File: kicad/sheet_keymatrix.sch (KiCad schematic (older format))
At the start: 67 parts, among them SW10 SW_Push, SW11 SW_Push, SW12 SW_Push, SW13 SW_Push, SW14 SW_Push, SW15 SW_Push, SW16 SW_Push, SW17 SW_Push, SW18 SW_Push, SW19 SW_Push, SW2 SW_Push, SW20 SW_Push, SW21 SW_Push, SW22 SW_Push, SW23 SW_Push, SW24 SW_Push, SW25 SW_Push, SW26 SW_Push, SW27 SW_Push, SW28 SW_Push, SW29 SW_Push, SW3 SW_Push, SW30 SW_Push, SW31 SW_Push, SW32 SW_Push, SW33 SW_Push, SW34 SW_Push, SW35 SW_Push, SW36 SW_Push, SW37 SW_Push, SW38 SW_Push, SW39 SW_Push, SW4 SW_Push, SW40 SW_Push, SW41 SW_Push, SW42 SW_Push, SW43 SW_Push, SW44 SW_Push, SW45 SW_Push, SW46 SW_Push, SW47 SW_Push, SW48 SW_Push, SW49 SW_Push, SW5 SW_Push, SW50 SW_Push, SW51 SW_Push, SW52 SW_Push, SW53 SW_Push, SW6 SW_Push, SW7 SW_Push, SW8 SW_Push, SW9 SW_Push

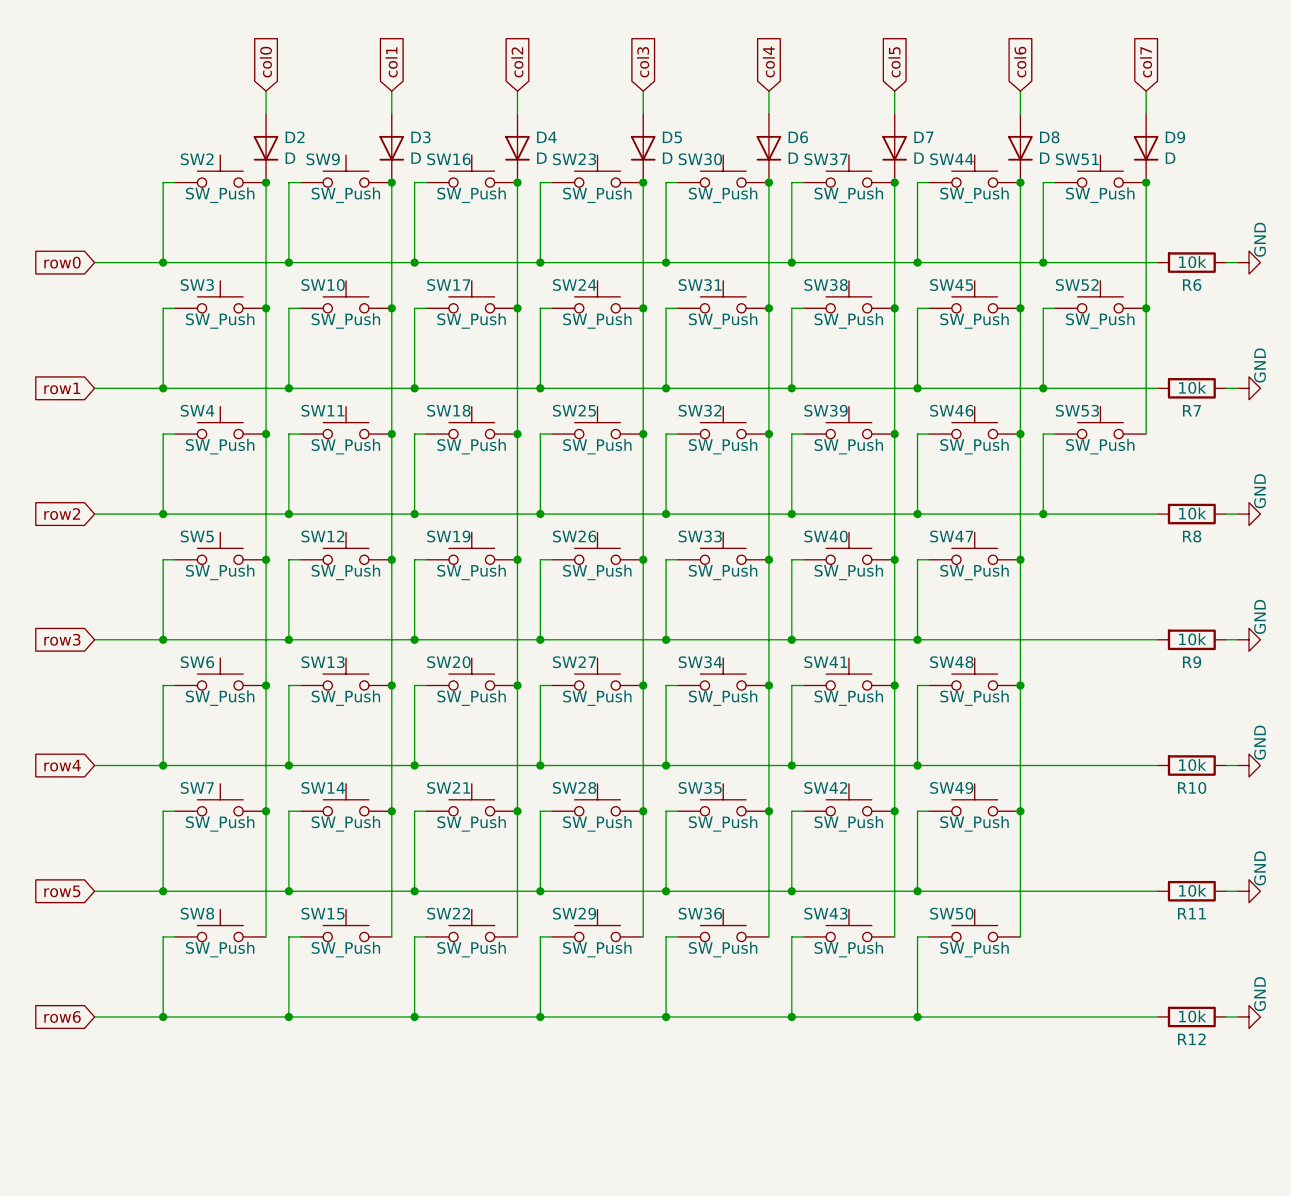
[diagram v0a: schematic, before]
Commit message: kicad: completed partial layout
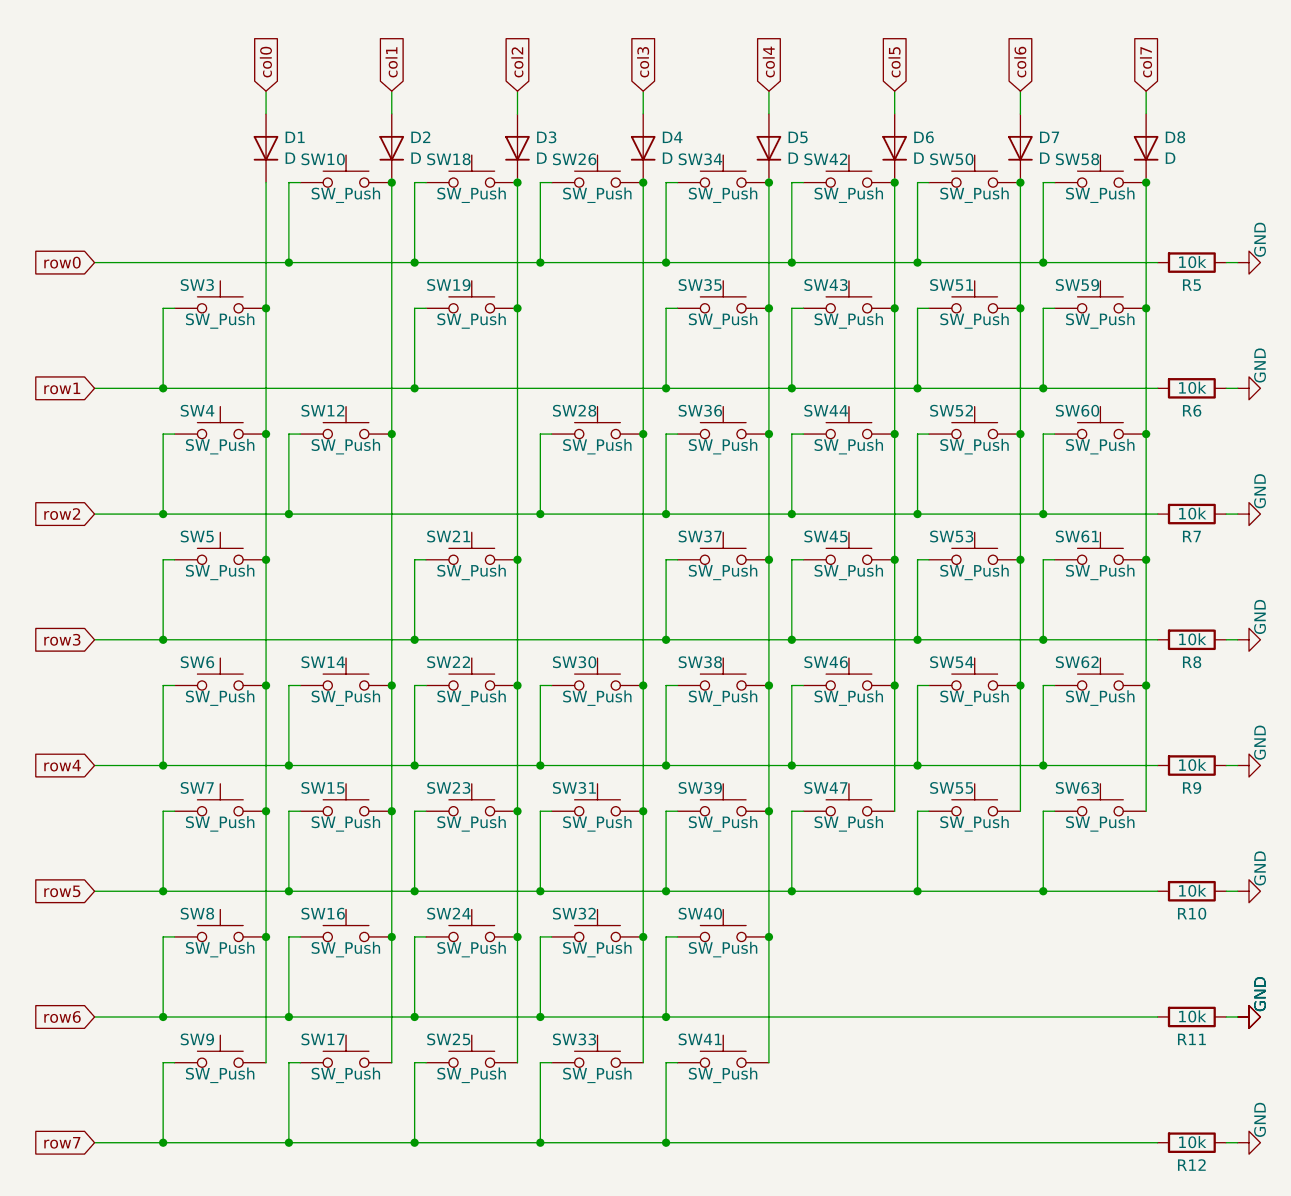
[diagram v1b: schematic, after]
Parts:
- removed SW10, SW12, SW2: SW_Push, pcb_buttons:btn_rect, symbol Switch:SW_Push
- removed SW18, SW24, SW26, SW43, SW50: SW_Push, pcb_buttons:btn_circular, symbol Switch:SW_Push
- added R12: 10k, Resistor_SMD:R_0603_1608Metric_Pad1.05x0.95mm_HandSolder, symbol Device:R
- added SW17, SW25, SW33, SW41, SW61, SW62, SW63, SW9: SW_Push, pcb_buttons:btn_circular, symbol Switch:SW_Push
- SW12: renamed from SW11; footprint pcb_buttons:btn_rect -> pcb_buttons:btn_long_rect
- SW14: renamed from SW13; footprint pcb_buttons:btn_rect -> pcb_buttons:btn_circular
- SW15: renamed from SW14; footprint pcb_buttons:btn_long_rect -> pcb_buttons:btn_circular
- SW16: renamed from SW15; footprint pcb_buttons:btn_long_rect -> pcb_buttons:btn_circular
- SW18: renamed from SW16; footprint pcb_buttons:btn_circular -> pcb_buttons:btn_rect
- SW19: renamed from SW17; footprint pcb_buttons:btn_circular -> pcb_buttons:btn_rect
- SW21: renamed from SW19; footprint pcb_buttons:btn_circular -> pcb_buttons:btn_rect
- SW26: renamed from SW23; footprint pcb_buttons:btn_circular -> pcb_buttons:btn_rect
- SW28: renamed from SW25; footprint pcb_buttons:btn_circular -> pcb_buttons:btn_long_rect
- SW34: renamed from SW30; footprint pcb_buttons:btn_circular -> pcb_buttons:btn_rect
- SW35: renamed from SW31; footprint pcb_buttons:btn_circular -> pcb_buttons:btn_rect
- SW36: renamed from SW32; footprint pcb_buttons:btn_circular -> pcb_buttons:btn_rect
- SW37: renamed from SW33; footprint pcb_buttons:btn_circular -> pcb_buttons:btn_rect
- SW6, SW7, SW8: footprint pcb_buttons:btn_rect -> pcb_buttons:btn_circular
- renumbered D2 to D1, D3 to D2, D4 to D3, D5 to D4, D6 to D5, D7 to D6, D8 to D7, D9 to D8, R11 to R10, R12 to R11, R6 to R5, R7 to R6, R8 to R7, R9 to R8, R10 to R9, SW9 to SW10, SW20 to SW22, SW21 to SW23, SW22 to SW24, SW27 to SW30, SW28 to SW31, SW29 to SW32, SW34 to SW38, SW35 to SW39, SW36 to SW40, SW37 to SW42, SW38 to SW43, SW39 to SW44, SW40 to SW45, SW41 to SW46, SW42 to SW47, SW44 to SW50, SW45 to SW51, SW46 to SW52, SW47 to SW53, SW48 to SW54, SW49 to SW55, SW51 to SW58, SW52 to SW59, SW53 to SW60
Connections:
- net GND: now also R12.1
- net row3: now also SW61.1
- net row4: now also SW62.1
- net row5: now also SW63.1
- net at D4.1 (K), SW26.2, SW28.2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: now also SW33.2
- net at D3.1 (K), SW18.2, SW19.2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: now also SW25.2
- net at D2.1 (K), SW10.2, SW12.2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: now also SW17.2
- net at D1.1 (K), SW3.2, SW4.2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: now also SW9.2
- net at D8.1 (K), SW58.2, SW59.2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: now also SW61.2, SW62.2, SW63.2
- net at D5.1 (K), SW34.2, SW35.2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: now also SW41.2
- new net row7: R12.2, SW17.1, SW25.1, SW33.1, SW41.1, SW9.1

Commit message: kicad: finalize device BOM
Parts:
- D1, D2, D3, D4, D5, D6, D7, D8: Description (none) -> Switch matrix protection; Digi-Key PN (none) -> TS4148CRZGCT-ND; Digi-Key Page (none) -> https://www.digikey.com/product-detail/en/taiwan-semiconduc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
- R10, R11, R12, R5, R6, R7, R8, R9: Description (none) -> Input pull-down resistor; Digi-Key PN (none) -> 311-10.0KHRCT-ND; Digi-Key Page (none) -> https://www.digikey.com/product-detail/en/yageo/RC0603FR-07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
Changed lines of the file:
@@
 F 1 "10k" V 5850 4850 50  0000 C CNN
 F 2 "Resistor_SMD:R_0603_1608Metric_Pad1.05x0.95mm_HandSolder" V 5780 4850 50  0001 C CNN
-F 3 "~" H 5850 4850 50  0001 C CNN
+F 3 "http://www.yageo.com/documents/recent/PYu-RC_Group_51_RoHS_L_10.pdf" H 5850 4850 50  0001 C CNN
+F 4 "Input pull-down resistor" H 5850 4850 50  0001 C CNN "Description"
+F 5 "311-10.0KHRCT-ND" H 5850 4850 50  0001 C CNN "Digi-Key PN"
+F 6 "https://www.digikey.com/product-detail/en/yageo/RC0603FR-0710KL/311-10.0KHRCT-ND/729827" H 5850 4850 50  0001 C CNN "Digi-Key Page"
 	1    5850 4850
 	0    1    1    0
@@
 F 1 "10k" V 5850 4300 50  0000 C CNN
 F 2 "Resistor_SMD:R_0603_1608Metric_Pad1.05x0.95mm_HandSolder" V 5780 4300 50  0001 C CNN
-F 3 "~" H 5850 4300 50  0001 C CNN
+F 3 "http://www.yageo.com/documents/recent/PYu-RC_Group_51_RoHS_L_10.pdf" H 5850 4300 50  0001 C CNN
+F 4 "Input pull-down resistor" H 5850 4300 50  0001 C CNN "Description"
+F 5 "311-10.0KHRCT-ND" H 5850 4300 50  0001 C CNN "Digi-Key PN"
+F 6 "https://www.digikey.com/product-detail/en/yageo/RC0603FR-0710KL/311-10.0KHRCT-ND/729827" H 5850 4300 50  0001 C CNN "Digi-Key Page"
 	1    5850 4300
 	0    1    1    0
@@
 F 1 "10k" V 5850 3750 50  0000 C CNN
 F 2 "Resistor_SMD:R_0603_1608Metric_Pad1.05x0.95mm_HandSolder" V 5780 3750 50  0001 C CNN
-F 3 "~" H 5850 3750 50  0001 C CNN
+F 3 "http://www.yageo.com/documents/recent/PYu-RC_Group_51_RoHS_L_10.pdf" H 5850 3750 50  0001 C CNN
+F 4 "Input pull-down resistor" H 5850 3750 50  0001 C CNN "Description"
+F 5 "311-10.0KHRCT-ND" H 5850 3750 50  0001 C CNN "Digi-Key PN"
+F 6 "https://www.digikey.com/product-detail/en/yageo/RC0603FR-0710KL/311-10.0KHRCT-ND/729827" H 5850 3750 50  0001 C CNN "Digi-Key Page"
 	1    5850 3750
 	0    1    1    0
@@
 F 1 "10k" V 5850 3200 50  0000 C CNN
 F 2 "Resistor_SMD:R_0603_1608Metric_Pad1.05x0.95mm_HandSolder" V 5780 3200 50  0001 C CNN
-F 3 "~" H 5850 3200 50  0001 C CNN
+F 3 "http://www.yageo.com/documents/recent/PYu-RC_Group_51_RoHS_L_10.pdf" H 5850 3200 50  0001 C CNN
+F 4 "Input pull-down resistor" H 5850 3200 50  0001 C CNN "Description"
+F 5 "311-10.0KHRCT-ND" H 5850 3200 50  0001 C CNN "Digi-Key PN"
+F 6 "https://www.digikey.com/product-detail/en/yageo/RC0603FR-0710KL/311-10.0KHRCT-ND/729827" H 5850 3200 50  0001 C CNN "Digi-Key Page"
 	1    5850 3200
 	0    1    1    0
@@
 F 1 "10k" V 5850 2650 50  0000 C CNN
 F 2 "Resistor_SMD:R_0603_1608Metric_Pad1.05x0.95mm_HandSolder" V 5780 2650 50  0001 C CNN
-F 3 "~" H 5850 2650 50  0001 C CNN
+F 3 "http://www.yageo.com/documents/recent/PYu-RC_Group_51_RoHS_L_10.pdf" H 5850 2650 50  0001 C CNN
+F 4 "Input pull-down resistor" H 5850 2650 50  0001 C CNN "Description"
+F 5 "311-10.0KHRCT-ND" H 5850 2650 50  0001 C CNN "Digi-Key PN"
+F 6 "https://www.digikey.com/product-detail/en/yageo/RC0603FR-0710KL/311-10.0KHRCT-ND/729827" H 5850 2650 50  0001 C CNN "Digi-Key Page"
 	1    5850 2650
 	0    1    1    0
@@
 F 1 "10k" V 5850 2100 50  0000 C CNN
 F 2 "Resistor_SMD:R_0603_1608Metric_Pad1.05x0.95mm_HandSolder" V 5780 2100 50  0001 C CNN
-F 3 "~" H 5850 2100 50  0001 C CNN
+F 3 "http://www.yageo.com/documents/recent/PYu-RC_Group_51_RoHS_L_10.pdf" H 5850 2100 50  0001 C CNN
+F 4 "Input pull-down resistor" H 5850 2100 50  0001 C CNN "Description"
+F 5 "311-10.0KHRCT-ND" H 5850 2100 50  0001 C CNN "Digi-Key PN"
+F 6 "https://www.digikey.com/product-detail/en/yageo/RC0603FR-0710KL/311-10.0KHRCT-ND/729827" H 5850 2100 50  0001 C CNN "Digi-Key Page"
 	1    5850 2100
 	0    1    1    0
@@
 F 1 "10k" V 5850 1550 50  0000 C CNN
 F 2 "Resistor_SMD:R_0603_1608Metric_Pad1.05x0.95mm_HandSolder" V 5780 1550 50  0001 C CNN
-F 3 "~" H 5850 1550 50  0001 C CNN
+F 3 "http://www.yageo.com/documents/recent/PYu-RC_Group_51_RoHS_L_10.pdf" H 5850 1550 50  0001 C CNN
+F 4 "Input pull-down resistor" H 5850 1550 50  0001 C CNN "Description"
+F 5 "311-10.0KHRCT-ND" H 5850 1550 50  0001 C CNN "Digi-Key PN"
+F 6 "https://www.digikey.com/product-detail/en/yageo/RC0603FR-0710KL/311-10.0KHRCT-ND/729827" H 5850 1550 50  0001 C CNN "Digi-Key Page"
 	1    5850 1550
 	0    1    1    0
@@
 F 1 "D" V 2855 971 50  0000 R CNN
 F 2 "Diode_SMD:D_0603_1608Metric_Pad1.05x0.95mm_HandSolder" H 2900 1050 50  0001 C CNN
-F 3 "~" H 2900 1050 50  0001 C CNN
+F 3 "https://www.taiwansemi.com/products/datasheet/TS4148C_G1809.pdf" H 2900 1050 50  0001 C CNN
+F 4 "Switch matrix protection" H 2900 1050 50  0001 C CNN "Description"
+F 5 "TS4148CRZGCT-ND" H 2900 1050 50  0001 C CNN "Digi-Key PN"
+F 6 "https://www.digikey.com/product-detail/en/taiwan-semiconductor-corporation/TS4148C-RZG/TS4148CRZGCT-ND/7359812" H 2900 1050 50  0001 C CNN "Digi-Key Page"
 	1    2900 1050
 	0    -1   -1   0
@@
 F 1 "D" V 3405 971 50  0000 R CNN
 F 2 "Diode_SMD:D_0603_1608Metric_Pad1.05x0.95mm_HandSolder" H 3450 1050 50  0001 C CNN
-F 3 "~" H 3450 1050 50  0001 C CNN
+F 3 "https://www.taiwansemi.com/products/datasheet/TS4148C_G1809.pdf" H 3450 1050 50  0001 C CNN
+F 4 "Switch matrix protection" H 3450 1050 50  0001 C CNN "Description"
+F 5 "TS4148CRZGCT-ND" H 3450 1050 50  0001 C CNN "Digi-Key PN"
+F 6 "https://www.digikey.com/product-detail/en/taiwan-semiconductor-corporation/TS4148C-RZG/TS4148CRZGCT-ND/7359812" H 3450 1050 50  0001 C CNN "Digi-Key Page"
 	1    3450 1050
 	0    -1   -1   0
@@
 F 1 "D" V 4505 971 50  0000 R CNN
 F 2 "Diode_SMD:D_0603_1608Metric_Pad1.05x0.95mm_HandSolder" H 4550 1050 50  0001 C CNN
-F 3 "~" H 4550 1050 50  0001 C CNN
+F 3 "https://www.taiwansemi.com/products/datasheet/TS4148C_G1809.pdf" H 4550 1050 50  0001 C CNN
+F 4 "Switch matrix protection" H 4550 1050 50  0001 C CNN "Description"
+F 5 "TS4148CRZGCT-ND" H 4550 1050 50  0001 C CNN "Digi-Key PN"
+F 6 "https://www.digikey.com/product-detail/en/taiwan-semiconductor-corporation/TS4148C-RZG/TS4148CRZGCT-ND/7359812" H 4550 1050 50  0001 C CNN "Digi-Key Page"
 	1    4550 1050
 	0    -1   -1   0
@@
 F 1 "D" V 5055 971 50  0000 R CNN
 F 2 "Diode_SMD:D_0603_1608Metric_Pad1.05x0.95mm_HandSolder" H 5100 1050 50  0001 C CNN
-F 3 "~" H 5100 1050 50  0001 C CNN
+F 3 "https://www.taiwansemi.com/products/datasheet/TS4148C_G1809.pdf" H 5100 1050 50  0001 C CNN
+F 4 "Switch matrix protection" H 5100 1050 50  0001 C CNN "Description"
+F 5 "TS4148CRZGCT-ND" H 5100 1050 50  0001 C CNN "Digi-Key PN"
+F 6 "https://www.digikey.com/product-detail/en/taiwan-semiconductor-corporation/TS4148C-RZG/TS4148CRZGCT-ND/7359812" H 5100 1050 50  0001 C CNN "Digi-Key Page"
 	1    5100 1050
 	0    -1   -1   0
@@
 F 1 "D" V 5605 971 50  0000 R CNN
 F 2 "Diode_SMD:D_0603_1608Metric_Pad1.05x0.95mm_HandSolder" H 5650 1050 50  0001 C CNN
-F 3 "~" H 5650 1050 50  0001 C CNN
+F 3 "https://www.taiwansemi.com/products/datasheet/TS4148C_G1809.pdf" H 5650 1050 50  0001 C CNN
+F 4 "Switch matrix protection" H 5650 1050 50  0001 C CNN "Description"
+F 5 "TS4148CRZGCT-ND" H 5650 1050 50  0001 C CNN "Digi-Key PN"
+F 6 "https://www.digikey.com/product-detail/en/taiwan-semiconductor-corporation/TS4148C-RZG/TS4148CRZGCT-ND/7359812" H 5650 1050 50  0001 C CNN "Digi-Key Page"
 	1    5650 1050
 	0    -1   -1   0
@@
 F 1 "D" V 2305 971 50  0000 R CNN
 F 2 "Diode_SMD:D_0603_1608Metric_Pad1.05x0.95mm_HandSolder" H 2350 1050 50  0001 C CNN
-F 3 "~" H 2350 1050 50  0001 C CNN
+F 3 "https://www.taiwansemi.com/products/datasheet/TS4148C_G1809.pdf" H 2350 1050 50  0001 C CNN
+F 4 "Switch matrix protection" H 2350 1050 50  0001 C CNN "Description"
+F 5 "TS4148CRZGCT-ND" H 2350 1050 50  0001 C CNN "Digi-Key PN"
+F 6 "https://www.digikey.com/product-detail/en/taiwan-semiconductor-corporation/TS4148C-RZG/TS4148CRZGCT-ND/7359812" H 2350 1050 50  0001 C CNN "Digi-Key Page"
 	1    2350 1050
 	0    -1   -1   0
@@
 F 1 "D" V 1755 971 50  0000 R CNN
 F 2 "Diode_SMD:D_0603_1608Metric_Pad1.05x0.95mm_HandSolder" H 1800 1050 50  0001 C CNN
-F 3 "~" H 1800 1050 50  0001 C CNN
+F 3 "https://www.taiwansemi.com/products/datasheet/TS4148C_G1809.pdf" H 1800 1050 50  0001 C CNN
+F 4 "Switch matrix protection" H 1800 1050 50  0001 C CNN "Description"
+F 5 "TS4148CRZGCT-ND" H 1800 1050 50  0001 C CNN "Digi-Key PN"
+F 6 "https://www.digikey.com/product-detail/en/taiwan-semiconductor-corporation/TS4148C-RZG/TS4148CRZGCT-ND/7359812" H 1800 1050 50  0001 C CNN "Digi-Key Page"
 	1    1800 1050
 	0    -1   -1   0
@@
 F 1 "D" V 3955 971 50  0000 R CNN
 F 2 "Diode_SMD:D_0603_1608Metric_Pad1.05x0.95mm_HandSolder" H 4000 1050 50  0001 C CNN
-F 3 "~" H 4000 1050 50  0001 C CNN
+F 3 "https://www.taiwansemi.com/products/datasheet/TS4148C_G1809.pdf" H 4000 1050 50  0001 C CNN
+F 4 "Switch matrix protection" H 4000 1050 50  0001 C CNN "Description"
+F 5 "TS4148CRZGCT-ND" H 4000 1050 50  0001 C CNN "Digi-Key PN"
+F 6 "https://www.digikey.com/product-detail/en/taiwan-semiconductor-corporation/TS4148C-RZG/TS4148CRZGCT-ND/7359812" H 4000 1050 50  0001 C CNN "Digi-Key Page"
 	1    4000 1050
 	0    -1   -1   0
@@
 F 1 "10k" V 5850 5400 50  0000 C CNN
 F 2 "Resistor_SMD:R_0603_1608Metric_Pad1.05x0.95mm_HandSolder" V 5780 5400 50  0001 C CNN
-F 3 "~" H 5850 5400 50  0001 C CNN
+F 3 "http://www.yageo.com/documents/recent/PYu-RC_Group_51_RoHS_L_10.pdf" H 5850 5400 50  0001 C CNN
+F 4 "Input pull-down resistor" H 5850 5400 50  0001 C CNN "Description"
+F 5 "311-10.0KHRCT-ND" H 5850 5400 50  0001 C CNN "Digi-Key PN"
+F 6 "https://www.digikey.com/product-detail/en/yageo/RC0603FR-0710KL/311-10.0KHRCT-ND/729827" H 5850 5400 50  0001 C CNN "Digi-Key Page"
 	1    5850 5400
 	0    1    1    0
